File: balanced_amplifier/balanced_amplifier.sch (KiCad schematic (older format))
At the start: 7 parts, among them J1 Conn_01x04_Male, J2 Conn_01x04_Male, J3 Screw_Terminal_01x03, J4 Conn_01x04_Male, J5 Conn_01x04_Male

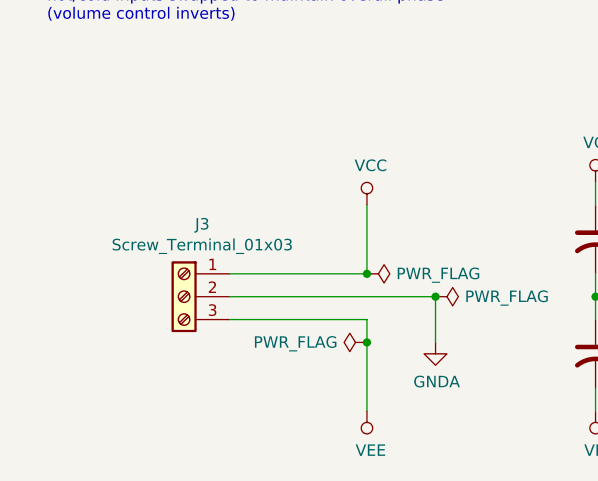
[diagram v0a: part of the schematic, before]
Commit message: complete initial layout of input section
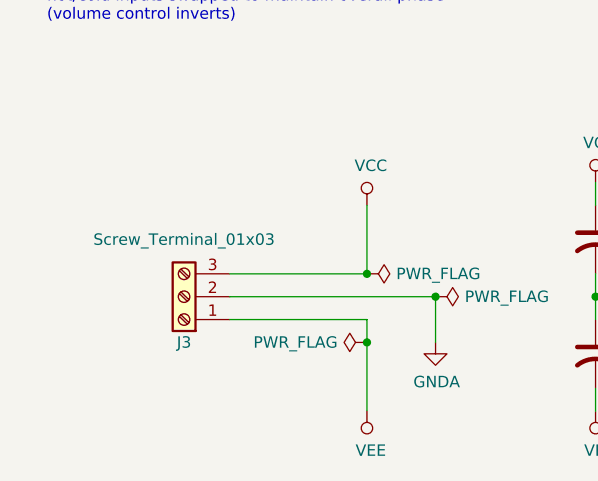
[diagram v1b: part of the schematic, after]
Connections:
- net VCC: now also J3.3 (Pin_3); no longer J3.1 (Pin_1)
- net VEE: now also J3.1 (Pin_1); no longer J3.3 (Pin_3)
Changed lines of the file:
@@
 U 1 1 5C512EBE
 P 1400 5300
-F 0 "J3" H 1320 5617 50  0000 C CNN
-F 1 "Screw_Terminal_01x03" H 1320 5526 50  0000 C CNN
+F 0 "J3" H 1400 5500 50  0000 C CNN
+F 1 "Screw_Terminal_01x03" H 1400 5050 50  0000 C CNN
 F 2 "TerminalBlock_Phoenix:TerminalBlock_Phoenix_PT-1,5-3-5.0-H_1x03_P5.00mm_Horizontal" H 1400 5300 50  0001 C CNN
 F 3 "https://media.digikey.com/pdf/Data%20Sheets/Phoenix%20Contact%20PDFs/1935174.pdf" H 1400 5300 50  0001 C CNN
@@
 F 9 "0.60" H 1400 5300 50  0001 C CNN "Unit Price"
 	1    1400 5300
-	-1   0    0    -1
+	-1   0    0    1
 $EndComp
 $Comp

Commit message: Update TODO list
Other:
- note added: "TODO:\nadd knobs for pots\nadd mounting holes"
- note removed: "TODO:\ncreate footprints for shrouded headers (Molex SL)\ncheck footprints for power connector\nadd knobs for pots"
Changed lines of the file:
@@
 	9300 3450 9200 3450
 Text Notes 1000 900  0    50   ~ 0
-TODO:\ncreate footprints for shrouded headers (Molex SL)\ncheck footprints for power connector\nadd knobs for pots
+TODO:\nadd knobs for pots\nadd mounting holes
 Text Label 1450 2600 0    50   ~ 0
 right_in_hot

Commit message: Add mounting holes to schematic
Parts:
- added H1, H2, H3, H4: MountingHole_Pad, MountingHole:MountingHole_4.5mm_Pad, symbol Mechanical:MountingHole_Pad
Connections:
- net GNDA: now also H1.1, H2.1, H3.1, H4.1
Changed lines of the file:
@@
 Wire Wire Line
 	2200 5500 2200 5400
+$Comp
+L Mechanical:MountingHole_Pad H2
+U 1 1 5C1B203E
+P 1400 6700
+F 0 "H2" H 1500 6751 50  0000 L CNN
+F 1 "MountingHole_Pad" H 1500 6660 50  0000 L CNN
+F 2 "MountingHole:MountingHole_4.5mm_Pad" H 1400 6700 50  0001 C CNN
+F 3 "~" H 1400 6700 50  0001 C CNN
+F 4 "~" H 1400 6700 50  0001 C CNN "Manufacturer"
+F 5 "~" H 1400 6700 50  0001 C CNN "Manufacturer PN"
+F 6 "~" H 1400 6700 50  0001 C CNN "Distributor"
+F 7 "~" H 1400 6700 50  0001 C CNN "Distributor PN"
+F 8 "~" H 1400 6700 50  0001 C CNN "URL"
+F 9 "~" H 1400 6700 50  0001 C CNN "Unit Price"
+	1    1400 6700
+	1    0    0    -1
+$EndComp
+$Comp
+L power:GNDA #PWR?
+U 1 1 5C1B223A
+P 1400 6800
+F 0 "#PWR?" H 1400 6550 50  0001 C CNN
+F 1 "GNDA" H 1405 6627 50  0000 C CNN
+F 2 "" H 1400 6800 50  0001 C CNN
+F 3 "" H 1400 6800 50  0001 C CNN
+	1    1400 6800
+	1    0    0    -1
+$EndComp
+$Comp
+L Mechanical:MountingHole_Pad H3
+U 1 1 5C1B2453
+P 1400 7150
+F 0 "H3" H 1500 7201 50  0000 L CNN
+F 1 "MountingHole_Pad" H 1500 7110 50  0000 L CNN
+F 2 "MountingHole:MountingHole_4.5mm_Pad" H 1400 7150 50  0001 C CNN
+F 3 "~" H 1400 7150 50  0001 C CNN
+F 4 "~" H 1400 7150 50  0001 C CNN "Manufacturer"
+F 5 "~" H 1400 7150 50  0001 C CNN "Manufacturer PN"
+F 6 "~" H 1400 7150 50  0001 C CNN "Distributor"
+F 7 "~" H 1400 7150 50  0001 C CNN "Distributor PN"
+F 8 "~" H 1400 7150 50  0001 C CNN "URL"
+F 9 "~" H 1400 7150 50  0001 C CNN "Unit Price"
+	1    1400 7150
+	1    0    0    -1
+$EndComp
+$Comp
+L power:GNDA #PWR?
+U 1 1 5C1B245A
+P 1400 7250
+F 0 "#PWR?" H 1400 7000 50  0001 C CNN
+F 1 "GNDA" H 1405 7077 50  0000 C CNN
+F 2 "" H 1400 7250 50  0001 C CNN
+F 3 "" H 1400 7250 50  0001 C CNN
+	1    1400 7250
+	1    0    0    -1
+$EndComp
+$Comp
+L Mechanical:MountingHole_Pad H4
+U 1 1 5C1B2D88
+P 1400 7600
+F 0 "H4" H 1500 7651 50  0000 L CNN
+F 1 "MountingHole_Pad" H 1500 7560 50  0000 L CNN
+F 2 "MountingHole:MountingHole_4.5mm_Pad" H 1400 7600 50  0001 C CNN
+F 3 "~" H 1400 7600 50  0001 C CNN
+F 4 "~" H 1400 7600 50  0001 C CNN "Manufacturer"
+F 5 "~" H 1400 7600 50  0001 C CNN "Manufacturer PN"
+F 6 "~" H 1400 7600 50  0001 C CNN "Distributor"
+F 7 "~" H 1400 7600 50  0001 C CNN "Distributor PN"
+F 8 "~" H 1400 7600 50  0001 C CNN "URL"
+F 9 "~" H 1400 7600 50  0001 C CNN "Unit Price"
+	1    1400 7600
+	1    0    0    -1
+$EndComp
+$Comp
+L power:GNDA #PWR?
+U 1 1 5C1B2D8F
+P 1400 7700
+F 0 "#PWR?" H 1400 7450 50  0001 C CNN
+F 1 "GNDA" H 1405 7527 50  0000 C CNN
+F 2 "" H 1400 7700 50  0001 C CNN
+F 3 "" H 1400 7700 50  0001 C CNN
+	1    1400 7700
+	1    0    0    -1
+$EndComp
+$Comp
+L Mechanical:MountingHole_Pad H1
+U 1 1 5C1B36D7
+P 1400 6250
+F 0 "H1" H 1500 6301 50  0000 L CNN
+F 1 "MountingHole_Pad" H 1500 6210 50  0000 L CNN
+F 2 "MountingHole:MountingHole_4.5mm_Pad" H 1400 6250 50  0001 C CNN
+F 3 "~" H 1400 6250 50  0001 C CNN
+F 4 "~" H 1400 6250 50  0001 C CNN "Manufacturer"
+F 5 "~" H 1400 6250 50  0001 C CNN "Manufacturer PN"
+F 6 "~" H 1400 6250 50  0001 C CNN "Distributor"
+F 7 "~" H 1400 6250 50  0001 C CNN "Distributor PN"
+F 8 "~" H 1400 6250 50  0001 C CNN "URL"
+F 9 "~" H 1400 6250 50  0001 C CNN "Unit Price"
+	1    1400 6250
+	1    0    0    -1
+$EndComp
+$Comp
+L power:GNDA #PWR?
+U 1 1 5C1B36DE
+P 1400 6350
+F 0 "#PWR?" H 1400 6100 50  0001 C CNN
+F 1 "GNDA" H 1405 6177 50  0000 C CNN
+F 2 "" H 1400 6350 50  0001 C CNN
+F 3 "" H 1400 6350 50  0001 C CNN
+	1    1400 6350
+	1    0    0    -1
+$EndComp
 $EndSCHEMATC

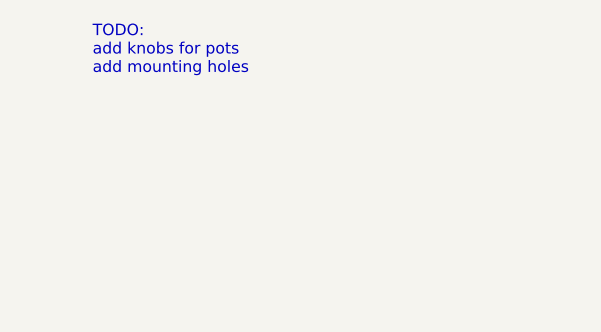
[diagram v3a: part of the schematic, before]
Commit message: Update TODO list (mounting holes added to PCB)
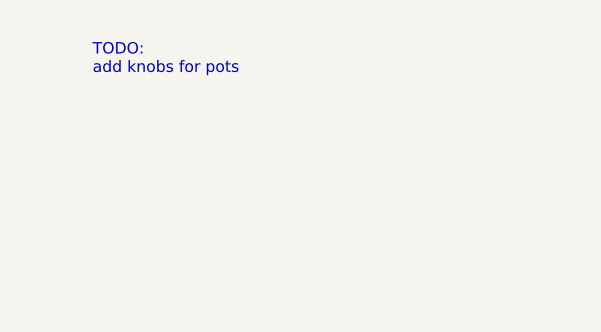
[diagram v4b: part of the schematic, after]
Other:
- note added: "TODO:\nadd knobs for pots"
- note removed: "TODO:\nadd knobs for pots\nadd mounting holes"
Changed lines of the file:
@@
 	9300 3450 9200 3450
 Text Notes 1000 900  0    50   ~ 0
-TODO:\nadd knobs for pots\nadd mounting holes
+TODO:\nadd knobs for pots
 Text Label 1450 2600 0    50   ~ 0
 right_in_hot
@@
 $EndComp
 $Comp
-L power:GNDA #PWR?
+L power:GNDA #PWR0137
 U 1 1 5C1B223A
 P 1400 6800
-F 0 "#PWR?" H 1400 6550 50  0001 C CNN
+F 0 "#PWR0137" H 1400 6550 50  0001 C CNN
 F 1 "GNDA" H 1405 6627 50  0000 C CNN
 F 2 "" H 1400 6800 50  0001 C CNN
@@
 $EndComp
 $Comp
-L power:GNDA #PWR?
+L power:GNDA #PWR0138
 U 1 1 5C1B245A
 P 1400 7250
-F 0 "#PWR?" H 1400 7000 50  0001 C CNN
+F 0 "#PWR0138" H 1400 7000 50  0001 C CNN
 F 1 "GNDA" H 1405 7077 50  0000 C CNN
 F 2 "" H 1400 7250 50  0001 C CNN
@@
 $EndComp
 $Comp
-L power:GNDA #PWR?
+L power:GNDA #PWR0139
 U 1 1 5C1B2D8F
 P 1400 7700
-F 0 "#PWR?" H 1400 7450 50  0001 C CNN
+F 0 "#PWR0139" H 1400 7450 50  0001 C CNN
 F 1 "GNDA" H 1405 7527 50  0000 C CNN
 F 2 "" H 1400 7700 50  0001 C CNN
@@
 $EndComp
 $Comp
-L power:GNDA #PWR?
+L power:GNDA #PWR0140
 U 1 1 5C1B36DE
 P 1400 6350
-F 0 "#PWR?" H 1400 6100 50  0001 C CNN
+F 0 "#PWR0140" H 1400 6100 50  0001 C CNN
 F 1 "GNDA" H 1405 6177 50  0000 C CNN
 F 2 "" H 1400 6350 50  0001 C CNN

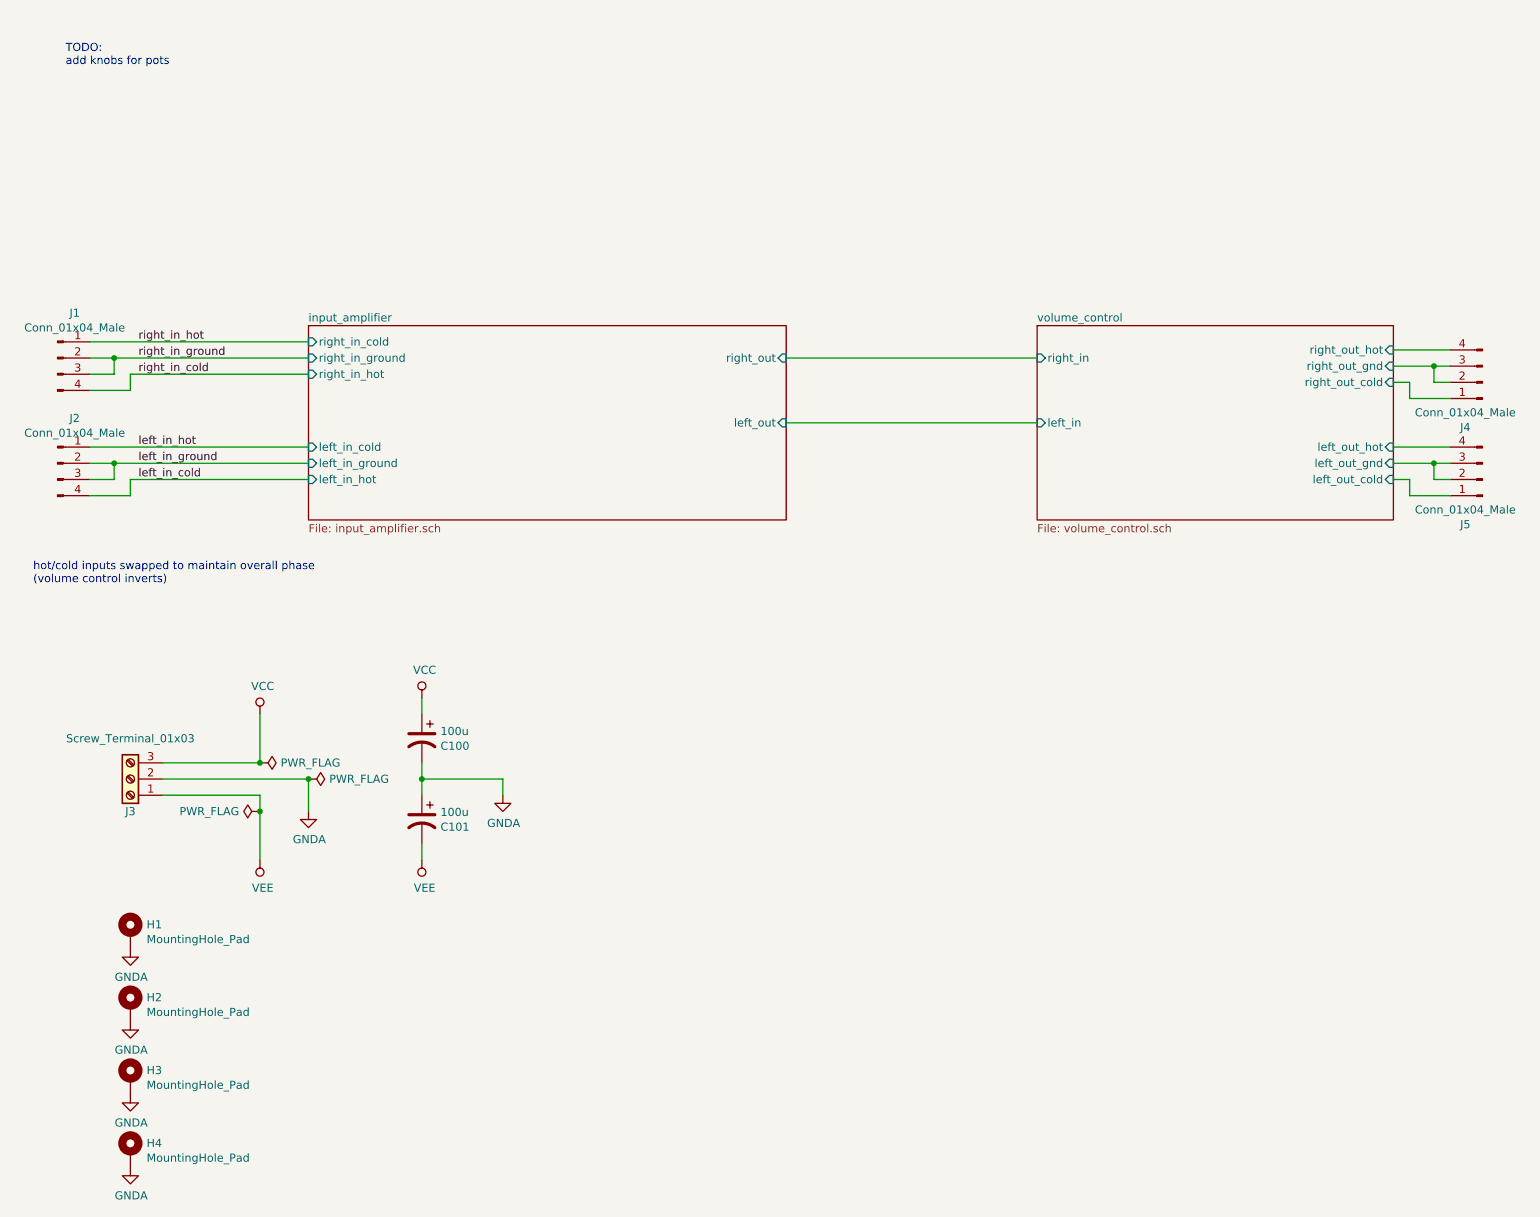
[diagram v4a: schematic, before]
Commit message: Add schematic annotation for hole size
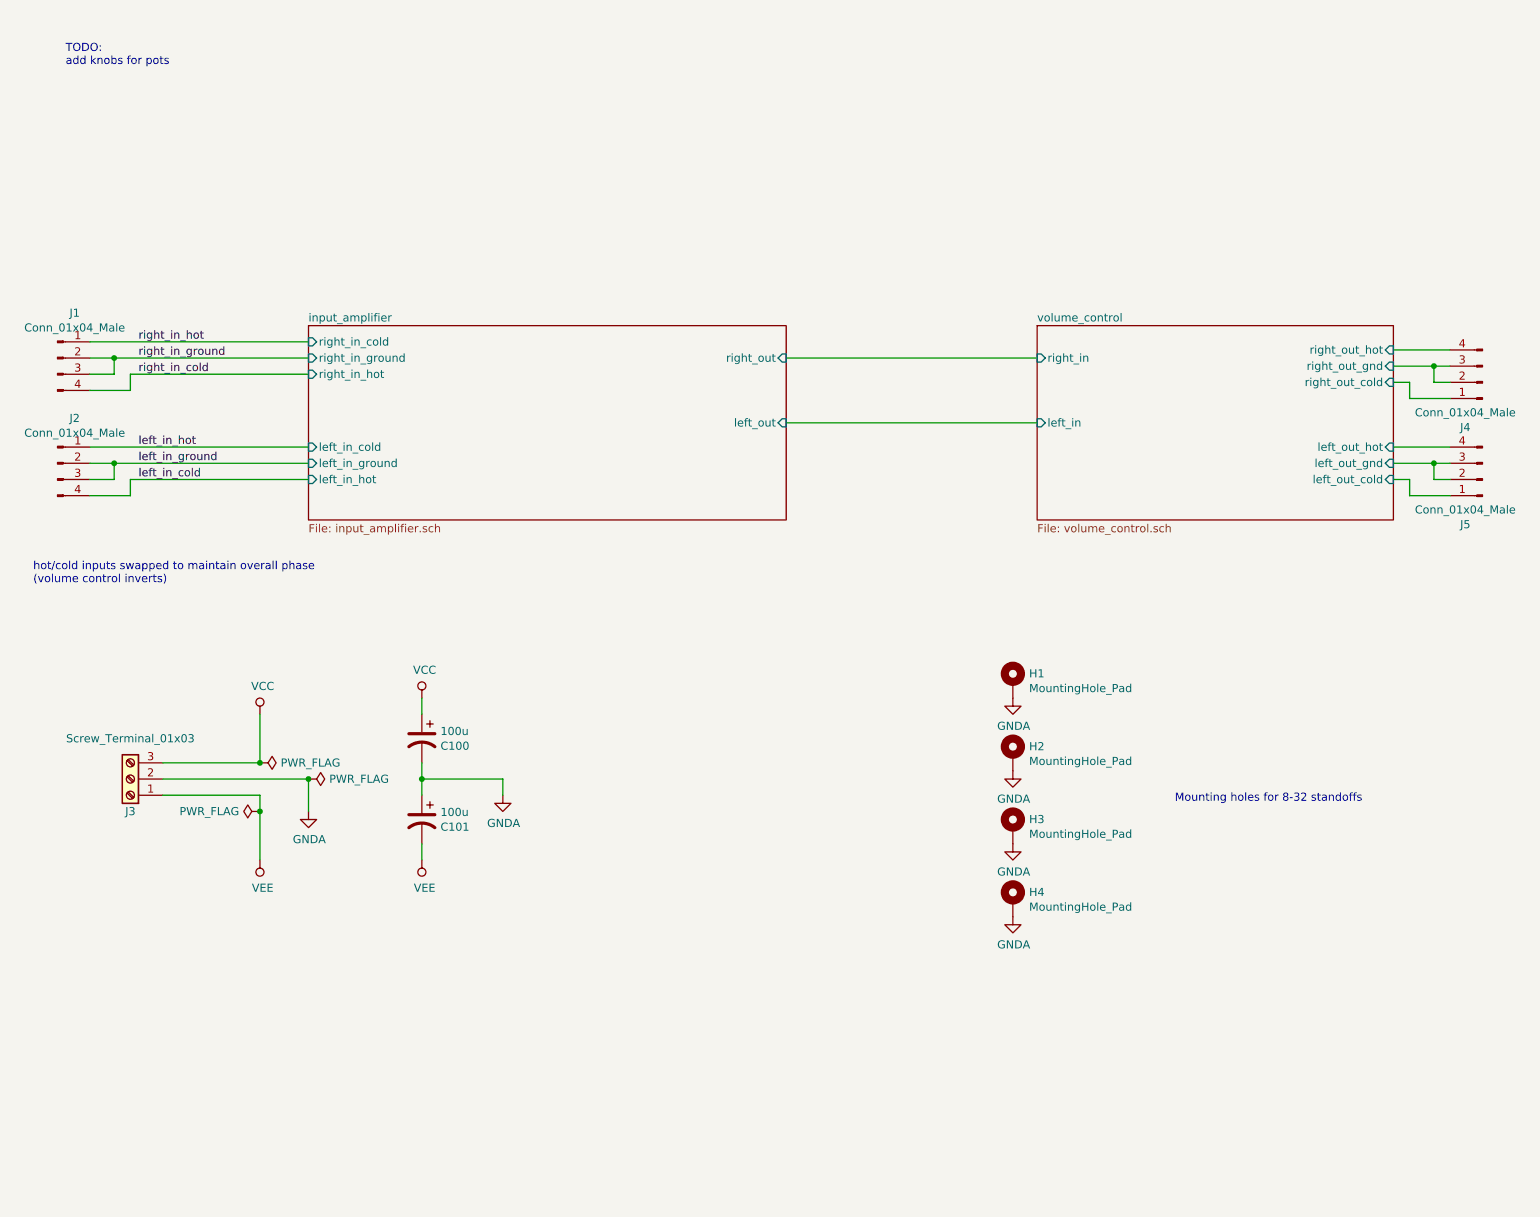
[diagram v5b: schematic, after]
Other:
- note added: "Mounting holes for 8-32 standoffs"
- moved on the sheet: H1, H2, H3, H4
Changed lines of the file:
@@
 L Mechanical:MountingHole_Pad H2
 U 1 1 5C1B203E
-P 1400 6700
-F 0 "H2" H 1500 6751 50  0000 L CNN
-F 1 "MountingHole_Pad" H 1500 6660 50  0000 L CNN
-F 2 "MountingHole:MountingHole_4.5mm_Pad" H 1400 6700 50  0001 C CNN
-F 3 "~" H 1400 6700 50  0001 C CNN
-F 4 "~" H 1400 6700 50  0001 C CNN "Manufacturer"
-F 5 "~" H 1400 6700 50  0001 C CNN "Manufacturer PN"
-F 6 "~" H 1400 6700 50  0001 C CNN "Distributor"
-F 7 "~" H 1400 6700 50  0001 C CNN "Distributor PN"
-F 8 "~" H 1400 6700 50  0001 C CNN "URL"
-F 9 "~" H 1400 6700 50  0001 C CNN "Unit Price"
-	1    1400 6700
+P 6850 5150
+F 0 "H2" H 6950 5201 50  0000 L CNN
+F 1 "MountingHole_Pad" H 6950 5110 50  0000 L CNN
+F 2 "MountingHole:MountingHole_4.5mm_Pad" H 6850 5150 50  0001 C CNN
+F 3 "~" H 6850 5150 50  0001 C CNN
+F 4 "~" H 6850 5150 50  0001 C CNN "Manufacturer"
+F 5 "~" H 6850 5150 50  0001 C CNN "Manufacturer PN"
+F 6 "~" H 6850 5150 50  0001 C CNN "Distributor"
+F 7 "~" H 6850 5150 50  0001 C CNN "Distributor PN"
+F 8 "~" H 6850 5150 50  0001 C CNN "URL"
+F 9 "~" H 6850 5150 50  0001 C CNN "Unit Price"
+	1    6850 5150
 	1    0    0    -1
 $EndComp
@@
 L power:GNDA #PWR0137
 U 1 1 5C1B223A
-P 1400 6800
-F 0 "#PWR0137" H 1400 6550 50  0001 C CNN
-F 1 "GNDA" H 1405 6627 50  0000 C CNN
-F 2 "" H 1400 6800 50  0001 C CNN
-F 3 "" H 1400 6800 50  0001 C CNN
-	1    1400 6800
+P 6850 5250
+F 0 "#PWR0137" H 6850 5000 50  0001 C CNN
+F 1 "GNDA" H 6855 5077 50  0000 C CNN
+F 2 "" H 6850 5250 50  0001 C CNN
+F 3 "" H 6850 5250 50  0001 C CNN
+	1    6850 5250
 	1    0    0    -1
 $EndComp
@@
 L Mechanical:MountingHole_Pad H3
 U 1 1 5C1B2453
-P 1400 7150
-F 0 "H3" H 1500 7201 50  0000 L CNN
-F 1 "MountingHole_Pad" H 1500 7110 50  0000 L CNN
-F 2 "MountingHole:MountingHole_4.5mm_Pad" H 1400 7150 50  0001 C CNN
-F 3 "~" H 1400 7150 50  0001 C CNN
-F 4 "~" H 1400 7150 50  0001 C CNN "Manufacturer"
-F 5 "~" H 1400 7150 50  0001 C CNN "Manufacturer PN"
-F 6 "~" H 1400 7150 50  0001 C CNN "Distributor"
-F 7 "~" H 1400 7150 50  0001 C CNN "Distributor PN"
-F 8 "~" H 1400 7150 50  0001 C CNN "URL"
-F 9 "~" H 1400 7150 50  0001 C CNN "Unit Price"
-	1    1400 7150
+P 6850 5600
+F 0 "H3" H 6950 5651 50  0000 L CNN
+F 1 "MountingHole_Pad" H 6950 5560 50  0000 L CNN
+F 2 "MountingHole:MountingHole_4.5mm_Pad" H 6850 5600 50  0001 C CNN
+F 3 "~" H 6850 5600 50  0001 C CNN
+F 4 "~" H 6850 5600 50  0001 C CNN "Manufacturer"
+F 5 "~" H 6850 5600 50  0001 C CNN "Manufacturer PN"
+F 6 "~" H 6850 5600 50  0001 C CNN "Distributor"
+F 7 "~" H 6850 5600 50  0001 C CNN "Distributor PN"
+F 8 "~" H 6850 5600 50  0001 C CNN "URL"
+F 9 "~" H 6850 5600 50  0001 C CNN "Unit Price"
+	1    6850 5600
 	1    0    0    -1
 $EndComp
@@
 L power:GNDA #PWR0138
 U 1 1 5C1B245A
-P 1400 7250
-F 0 "#PWR0138" H 1400 7000 50  0001 C CNN
-F 1 "GNDA" H 1405 7077 50  0000 C CNN
-F 2 "" H 1400 7250 50  0001 C CNN
-F 3 "" H 1400 7250 50  0001 C CNN
-	1    1400 7250
+P 6850 5700
+F 0 "#PWR0138" H 6850 5450 50  0001 C CNN
+F 1 "GNDA" H 6855 5527 50  0000 C CNN
+F 2 "" H 6850 5700 50  0001 C CNN
+F 3 "" H 6850 5700 50  0001 C CNN
+	1    6850 5700
 	1    0    0    -1
 $EndComp
@@
 L Mechanical:MountingHole_Pad H4
 U 1 1 5C1B2D88
-P 1400 7600
-F 0 "H4" H 1500 7651 50  0000 L CNN
-F 1 "MountingHole_Pad" H 1500 7560 50  0000 L CNN
-F 2 "MountingHole:MountingHole_4.5mm_Pad" H 1400 7600 50  0001 C CNN
-F 3 "~" H 1400 7600 50  0001 C CNN
-F 4 "~" H 1400 7600 50  0001 C CNN "Manufacturer"
-F 5 "~" H 1400 7600 50  0001 C CNN "Manufacturer PN"
-F 6 "~" H 1400 7600 50  0001 C CNN "Distributor"
-F 7 "~" H 1400 7600 50  0001 C CNN "Distributor PN"
-F 8 "~" H 1400 7600 50  0001 C CNN "URL"
-F 9 "~" H 1400 7600 50  0001 C CNN "Unit Price"
-	1    1400 7600
+P 6850 6050
+F 0 "H4" H 6950 6101 50  0000 L CNN
+F 1 "MountingHole_Pad" H 6950 6010 50  0000 L CNN
+F 2 "MountingHole:MountingHole_4.5mm_Pad" H 6850 6050 50  0001 C CNN
+F 3 "~" H 6850 6050 50  0001 C CNN
+F 4 "~" H 6850 6050 50  0001 C CNN "Manufacturer"
+F 5 "~" H 6850 6050 50  0001 C CNN "Manufacturer PN"
+F 6 "~" H 6850 6050 50  0001 C CNN "Distributor"
+F 7 "~" H 6850 6050 50  0001 C CNN "Distributor PN"
+F 8 "~" H 6850 6050 50  0001 C CNN "URL"
+F 9 "~" H 6850 6050 50  0001 C CNN "Unit Price"
+	1    6850 6050
 	1    0    0    -1
 $EndComp
@@
 L power:GNDA #PWR0139
 U 1 1 5C1B2D8F
-P 1400 7700
-F 0 "#PWR0139" H 1400 7450 50  0001 C CNN
-F 1 "GNDA" H 1405 7527 50  0000 C CNN
-F 2 "" H 1400 7700 50  0001 C CNN
-F 3 "" H 1400 7700 50  0001 C CNN
-	1    1400 7700
+P 6850 6150
+F 0 "#PWR0139" H 6850 5900 50  0001 C CNN
+F 1 "GNDA" H 6855 5977 50  0000 C CNN
+F 2 "" H 6850 6150 50  0001 C CNN
+F 3 "" H 6850 6150 50  0001 C CNN
+	1    6850 6150
 	1    0    0    -1
 $EndComp
@@
 L Mechanical:MountingHole_Pad H1
 U 1 1 5C1B36D7
-P 1400 6250
-F 0 "H1" H 1500 6301 50  0000 L CNN
-F 1 "MountingHole_Pad" H 1500 6210 50  0000 L CNN
-F 2 "MountingHole:MountingHole_4.5mm_Pad" H 1400 6250 50  0001 C CNN
-F 3 "~" H 1400 6250 50  0001 C CNN
-F 4 "~" H 1400 6250 50  0001 C CNN "Manufacturer"
-F 5 "~" H 1400 6250 50  0001 C CNN "Manufacturer PN"
-F 6 "~" H 1400 6250 50  0001 C CNN "Distributor"
-F 7 "~" H 1400 6250 50  0001 C CNN "Distributor PN"
-F 8 "~" H 1400 6250 50  0001 C CNN "URL"
-F 9 "~" H 1400 6250 50  0001 C CNN "Unit Price"
-	1    1400 6250
+P 6850 4700
+F 0 "H1" H 6950 4751 50  0000 L CNN
+F 1 "MountingHole_Pad" H 6950 4660 50  0000 L CNN
+F 2 "MountingHole:MountingHole_4.5mm_Pad" H 6850 4700 50  0001 C CNN
+F 3 "~" H 6850 4700 50  0001 C CNN
+F 4 "~" H 6850 4700 50  0001 C CNN "Manufacturer"
+F 5 "~" H 6850 4700 50  0001 C CNN "Manufacturer PN"
+F 6 "~" H 6850 4700 50  0001 C CNN "Distributor"
+F 7 "~" H 6850 4700 50  0001 C CNN "Distributor PN"
+F 8 "~" H 6850 4700 50  0001 C CNN "URL"
+F 9 "~" H 6850 4700 50  0001 C CNN "Unit Price"
+	1    6850 4700
 	1    0    0    -1
 $EndComp
@@
 L power:GNDA #PWR0140
 U 1 1 5C1B36DE
-P 1400 6350
-F 0 "#PWR0140" H 1400 6100 50  0001 C CNN
-F 1 "GNDA" H 1405 6177 50  0000 C CNN
-F 2 "" H 1400 6350 50  0001 C CNN
-F 3 "" H 1400 6350 50  0001 C CNN
-	1    1400 6350
+P 6850 4800
+F 0 "#PWR0140" H 6850 4550 50  0001 C CNN
+F 1 "GNDA" H 6855 4627 50  0000 C CNN
+F 2 "" H 6850 4800 50  0001 C CNN
+F 3 "" H 6850 4800 50  0001 C CNN
+	1    6850 4800
 	1    0    0    -1
 $EndComp
+Text Notes 7850 5450 0    50   ~ 0
+Mounting holes for 8-32 standoffs
 $EndSCHEMATC
